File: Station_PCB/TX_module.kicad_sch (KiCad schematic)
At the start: 6 parts, among them J10 Conn_01x04_Socket, J11 Conn_01x06_Socket, J6 Conn_01x19_Socket, J7 Conn_01x19_Socket, J8 Conn_01x08_Socket, J9 Conn_01x08_Socket

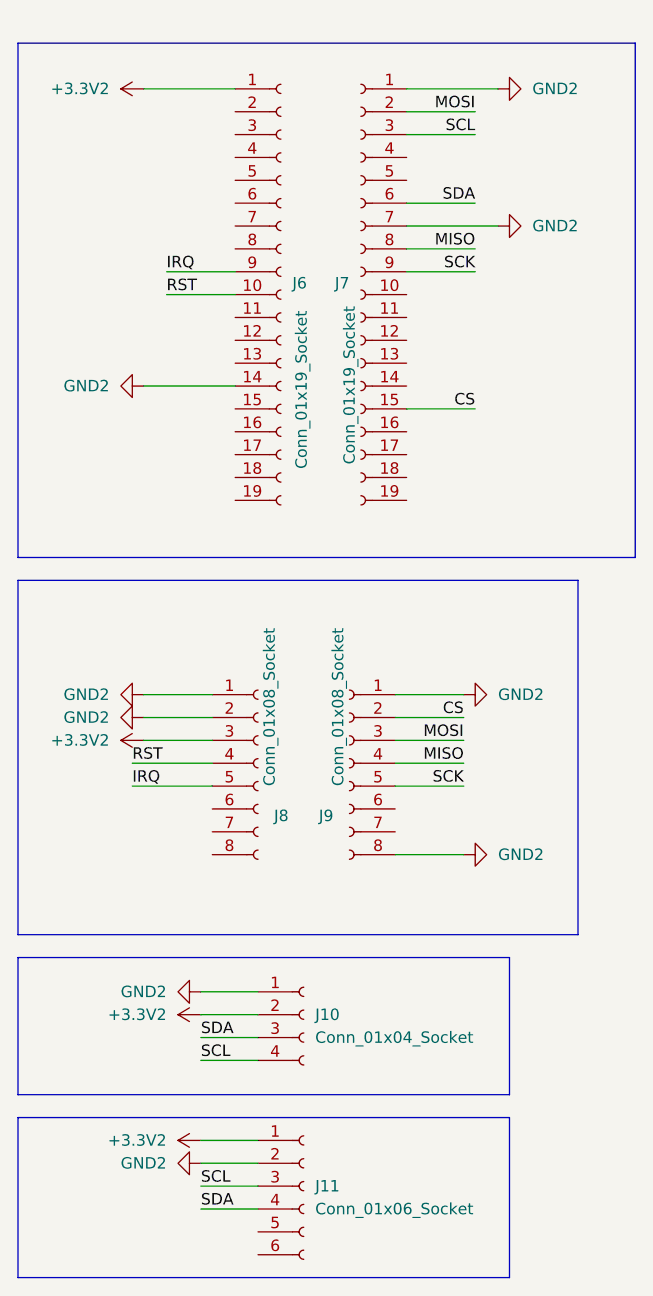
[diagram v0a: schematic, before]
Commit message: Mejora placa y la deja en una sola cara para impresion
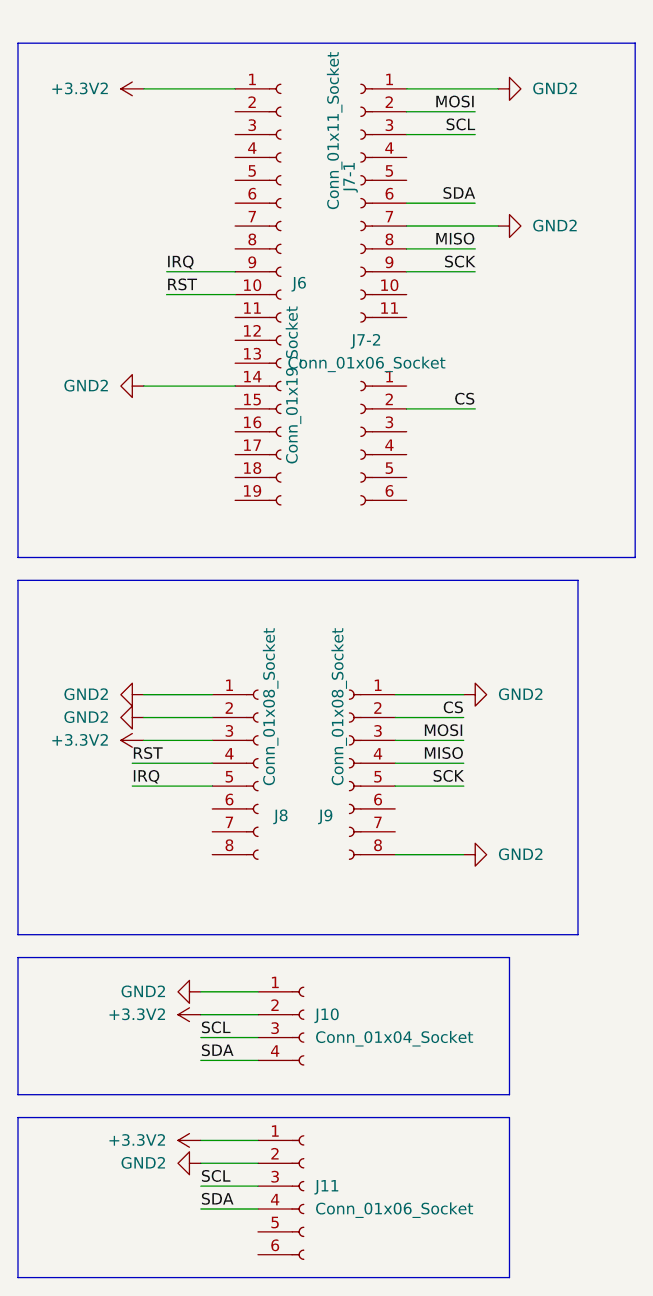
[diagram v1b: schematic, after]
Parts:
- removed J6: Conn_01x19_Socket, Connector_PinSocket_2.54mm:PinSocket_1x19_P2.54mm_Vertical, symbol Connector:Conn_01x19_Socket
- added J7-1: Conn_01x11_Socket, Connector_PinSocket_2.54mm:PinSocket_1x11_P2.54mm_Vertical, symbol Connector:Conn_01x11_Socket
- added J7-2: Conn_01x06_Socket, Connector_PinSocket_2.54mm:PinSocket_1x06_P2.54mm_Vertical, symbol Connector:Conn_01x06_Socket
- renumbered J7 to J6
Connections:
- net +3.3V2: now also J6.1 (Pin_1)
- net CS: now also J7-2.2 (Pin_2); no longer J6.15 (Pin_15)
- net GND2: now also J6.14 (Pin_14), J7-1.1 (Pin_1), J7-1.7 (Pin_7); no longer J6.1 (Pin_1), J6.7 (Pin_7)
- net IRQ: now also J6.9 (Pin_9)
- net MISO: now also J7-1.8 (Pin_8); no longer J6.8 (Pin_8)
- net MOSI: now also J7-1.2 (Pin_2); no longer J6.2 (Pin_2)
- net RST: now also J6.10 (Pin_10)
- net SCK: now also J7-1.9 (Pin_9); no longer J6.9 (Pin_9)
- net SCL: now also J10.3 (Pin_3), J7-1.3 (Pin_3); no longer J10.4 (Pin_4), J6.3 (Pin_3)
- net SDA: now also J10.4 (Pin_4), J7-1.6 (Pin_6); no longer J10.3 (Pin_3), J6.6 (Pin_6)
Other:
- moved on the sheet: J6
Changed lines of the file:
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@@
 	(wire
 		(pts
-			(xy 83.82 69.85) (xy 76.2 69.85)
+			(xy 45.72 109.22) (xy 54.61 109.22)
 		)
 		(stroke
@@
 	(wire
 		(pts
-			(xy 45.72 109.22) (xy 54.61 109.22)
+			(xy 74.93 106.68) (xy 82.55 106.68)
 		)
 		(stroke
@@
 	(wire
 		(pts
-			(xy 74.93 106.68) (xy 82.55 106.68)
+			(xy 46.99 106.68) (xy 54.61 106.68)
 		)
 		(stroke
@@
 	(wire
 		(pts
-			(xy 46.99 106.68) (xy 54.61 106.68)
+			(xy 74.93 101.6) (xy 82.55 101.6)
 		)
 		(stroke
@@
 	(wire
 		(pts
-			(xy 74.93 101.6) (xy 82.55 101.6)
+			(xy 57.15 67.31) (xy 46.99 67.31)
 		)
 		(stroke
@@
 	(wire
 		(pts
-			(xy 57.15 67.31) (xy 46.99 67.31)
+			(xy 76.2 69.85) (xy 83.82 69.85)
 		)
 		(stroke
@@
 		)
 	)
+	(label "SDA"
+		(at 53.34 142.24 0)
+		(effects
+			(font
+				(size 1.27 1.27)
+			)
+			(justify left bottom)
+		)
+	)
 	(label "CS"
 		(at 82.55 104.14 180)
@@
 	)
 	(label "SCL"
-		(at 53.34 142.24 0)
+		(at 53.34 139.7 0)
 		(effects
 			(font
@@
 	(label "IRQ"
 		(at 45.72 111.76 0)
-		(effects
-			(font
-				(size 1.27 1.27)
-			)
-			(justify left bottom)
-		)
-	)
-	(label "SDA"
-		(at 53.34 139.7 0)
 		(effects
 			(font
@@
 	)
 	(symbol
+		(lib_id "Connector:Conn_01x06_Socket")
+		(at 71.12 72.39 0)
+		(mirror y)
+		(unit 1)
+		(exclude_from_sim no)
+		(in_bom yes)
+		(on_board yes)
+		(dnp no)
+		(fields_autoplaced yes)
+		(property "Reference" "J7-2"
+			(at 71.755 62.23 0)
+			(effects
+				(font
+					(size 1.27 1.27)
+				)
+			)
+		)
+		(property "Value" "Conn_01x06_Socket"
+			(at 71.755 64.77 0)
+			(effects
+				(font
+					(size 1.27 1.27)
+				)
+			)
+		)
+		(property "Footprint" "Connector_PinSocket_2.54mm:PinSocket_1x06_P2.54mm_Vertical"
+			(at 71.12 72.39 0)
+			(effects
+				(font
+					(size 1.27 1.27)
+				)
+				(hide yes)
+			)
+		)
+		(property "Datasheet" "~"
+			(at 71.12 72.39 0)
+			(effects
+				(font
+					(size 1.27 1.27)
+				)
+				(hide yes)
+			)
+		)
+		(property "Description" "Generic connector, single row, 01x06, script generated"
+			(at 71.12 72.39 0)
+			(effects
+				(font
+					(size 1.27 1.27)
+				)
+				(hide yes)
+			)
+		)
+		(pin "6"
+		)
+		(pin "3"
+		)
+		(pin "5"
+		)
+		(pin "1"
+		)
+		(pin "2"
+		)
+		(pin "4"
+		)
+		(instances
+			(project ""
+				(path "/271bf7de-d7e3-4005-aae9-764829dfc76c/3ad789be-31fe-48dc-b262-8c72b4039f89"
+					(reference "J7-2")
+					(unit 1)
+				)
+			)
+		)
+	)
+	(symbol
 		(lib_id "power:GND")
 		(at 82.55 101.6 90)
@@
 	(symbol
 		(lib_id "Connector:Conn_01x19_Socket")
-		(at 71.12 57.15 0)
-		(mirror y)
-		(unit 1)
-		(exclude_from_sim no)
-		(in_bom yes)
-		(on_board yes)
-		(dnp no)
-		(property "Reference" "J7"
-			(at 69.85 55.8799 0)
+		(at 62.23 57.15 0)
+		(unit 1)
+		(exclude_from_sim no)
+		(in_bom yes)
+		(on_board yes)
+		(dnp no)
+		(property "Reference" "J6"
+			(at 63.5 55.8799 0)
 			(effects
 				(font
@@
 		)
 		(property "Value" "Conn_01x19_Socket"
-			(at 69.85 58.4199 90)
+			(at 63.5 58.4199 90)
 			(effects
 				(font
@@
 		)
 		(property "Footprint" "Connector_PinSocket_2.54mm:PinSocket_1x19_P2.54mm_Vertical"
-			(at 71.12 57.15 0)
+			(at 62.23 57.15 0)
 			(effects
 				(font
@@
 		)
 		(property "Datasheet" "~"
-			(at 71.12 57.15 0)
+			(at 62.23 57.15 0)
 			(effects
 				(font
@@
 		)
 		(property "Description" "Generic connector, single row, 01x19, script generated"
-			(at 71.12 57.15 0)
+			(at 62.23 57.15 0)
 			(effects
 				(font
@@
 			(project "Station_PCB"
 				(path "/271bf7de-d7e3-4005-aae9-764829dfc76c/3ad789be-31fe-48dc-b262-8c72b4039f89"
-					(reference "J7")
+					(reference "J6")
 					(unit 1)
 				)
@@
 	)
 	(symbol
-		(lib_id "Connector:Conn_01x19_Socket")
-		(at 62.23 57.15 0)
-		(unit 1)
-		(exclude_from_sim no)
-		(in_bom yes)
-		(on_board yes)
-		(dnp no)
-		(property "Reference" "J6"
-			(at 63.5 55.8799 0)
-			(effects
-				(font
-					(size 1.27 1.27)
-				)
-				(justify left)
-			)
-		)
-		(property "Value" "Conn_01x19_Socket"
-			(at 64.516 58.928 90)
-			(effects
-				(font
-					(size 1.27 1.27)
-				)
-				(justify right)
-			)
-		)
-		(property "Footprint" "Connector_PinSocket_2.54mm:PinSocket_1x19_P2.54mm_Vertical"
-			(at 62.23 57.15 0)
-			(effects
-				(font
-					(size 1.27 1.27)
-				)
-				(hide yes)
-			)
-		)
-		(property "Datasheet" "~"
-			(at 62.23 57.15 0)
-			(effects
-				(font
-					(size 1.27 1.27)
-				)
-				(hide yes)
-			)
-		)
-		(property "Description" "Generic connector, single row, 01x19, script generated"
-			(at 62.23 57.15 0)
-			(effects
-				(font
-					(size 1.27 1.27)
-				)
-				(hide yes)
-			)
-		)
-		(pin "6"
-		)
-		(pin "1"
-		)
-		(pin "14"
-		)
-		(pin "8"
-		)
-		(pin "15"
-		)
-		(pin "5"
-		)
-		(pin "10"
-		)
-		(pin "12"
-		)
-		(pin "19"
-		)
-		(pin "11"
-		)
-		(pin "17"
-		)
-		(pin "9"
-		)
-		(pin "18"
-		)
-		(pin "4"
-		)
-		(pin "2"
-		)
-		(pin "16"
-		)
-		(pin "13"
-		)
-		(pin "7"
-		)
-		(pin "3"
-		)
-		(instances
-			(project "Station_PCB"
-				(path "/271bf7de-d7e3-4005-aae9-764829dfc76c/3ad789be-31fe-48dc-b262-8c72b4039f89"
-					(reference "J6")
-					(unit 1)
-				)
-			)
-		)
-	)
-	(symbol
 		(lib_id "Connector:Conn_01x06_Socket")
 		(at 64.77 156.21 0)
@@
 					(unit 1)
 				)
+			)
+		)
+	)
+	(symbol
+		(lib_id "Connector:Conn_01x11_Socket")
+		(at 71.12 46.99 0)
+		(mirror y)
+		(unit 1)
+		(exclude_from_sim no)
+		(in_bom yes)
+		(on_board yes)
+		(dnp no)
+		(property "Reference" "J7-1"
+			(at 69.85 45.7199 90)
+			(effects
+				(font
+					(size 1.27 1.27)
+				)
+				(justify left)
+			)
+		)
+		(property "Value" "Conn_01x11_Socket"
+			(at 68.072 47.752 90)
+			(effects
+				(font
+					(size 1.27 1.27)
+				)
+				(justify left)
+			)
+		)
+		(property "Footprint" "Connector_PinSocket_2.54mm:PinSocket_1x11_P2.54mm_Vertical"
+			(at 71.12 46.99 0)
+			(effects
+				(font
+					(size 1.27 1.27)
+				)
+				(hide yes)
+			)
+		)
+		(property "Datasheet" "~"
+			(at 71.12 46.99 0)
+			(effects
+				(font
+					(size 1.27 1.27)
+				)
+				(hide yes)
+			)
+		)
+		(property "Description" "Generic connector, single row, 01x11, script generated"
+			(at 71.12 46.99 0)
+			(effects
+				(font
+					(size 1.27 1.27)
+				)
+				(hide yes)
+			)
+		)
+		(pin "1"
+		)
+		(pin "2"
+		)
+		(pin "3"
+		)
+		(pin "7"
+		)
+		(pin "8"
+		)
+		(pin "6"
+		)
+		(pin "4"
+		)
+		(pin "9"
+		)
+		(pin "10"
+		)
+		(pin "5"
+		)
+		(pin "11"
+		)
+		(instances
+			(project "Station_PCB"
+				(path "/271bf7de-d7e3-4005-aae9-764829dfc76c/3ad789be-31fe-48dc-b262-8c72b4039f89"
+					(reference "J7-1")
+					(unit 1)
+				)
